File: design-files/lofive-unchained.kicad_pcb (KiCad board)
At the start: 4 copper layers, 35.6 x 17.8 mm, 39 parts, among them J1 Conn_01x09, J2 Conn_01x09, J3 USB_C_Receptacle_USB2.0, SW1 SW_Push, SW2 SW_Push, U1 ESP32-C3, U2 W25Q32JVZP, U3 TLV62569DRL, Y1 40Mhz

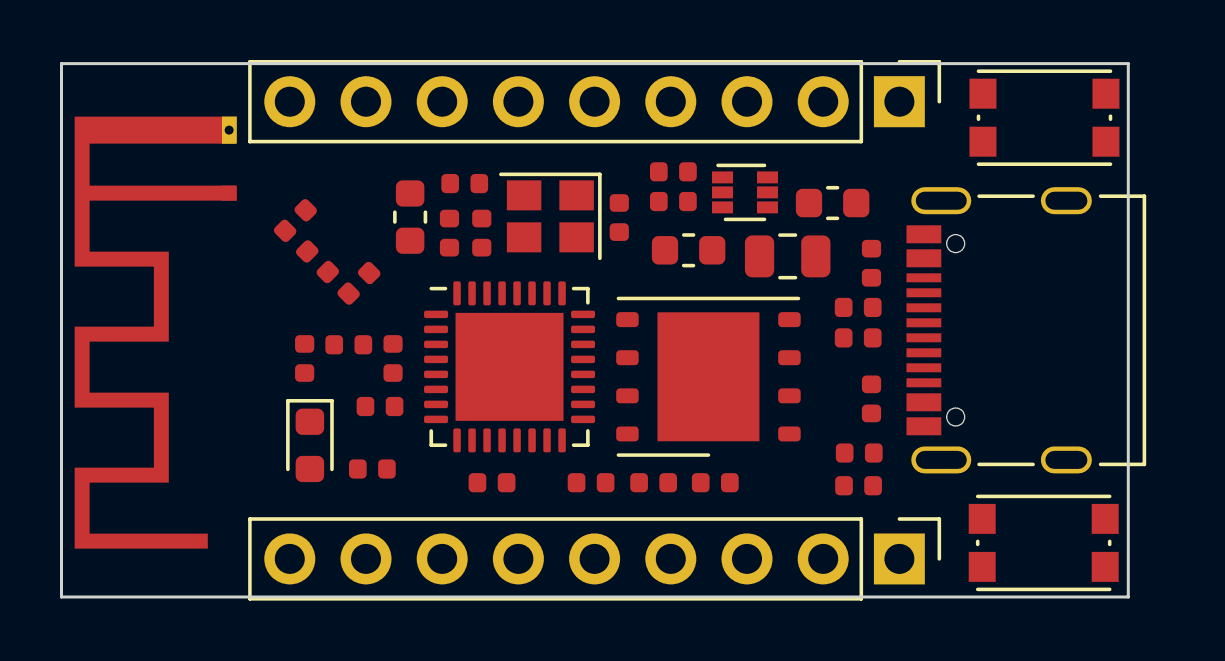
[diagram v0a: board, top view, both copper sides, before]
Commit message: Preliminary routing complete
Need to check the RF trace and USB routing.
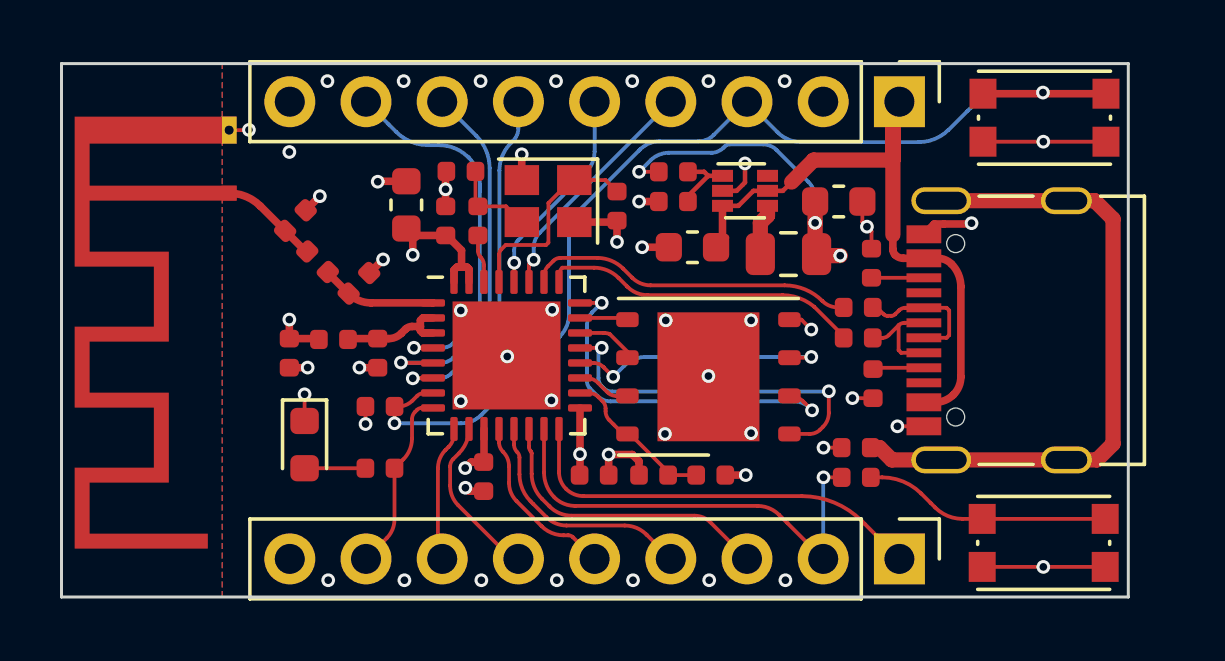
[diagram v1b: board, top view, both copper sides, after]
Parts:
- moved C6 0.54 mm to (122.3, 75.7)
- moved L1 0.54 mm to (120.8, 75.2)
- moved C3 0.54 mm to (119.4, 75.7)
- moved Y1 0.51 mm to (128.0, 70.6)
- moved R12 0.51 mm to (138.8, 76.7)
- moved C8 0.43 mm to (125.1, 69.6)
- moved R2 0.43 mm to (125.6, 71.3)
- moved C4 0.43 mm to (123.3, 70.8)
- moved C7 0.43 mm to (124.6, 71.3)
- moved U1 0.39 mm to (126.6, 75.8)
- moved C1 0.39 mm to (130.3, 70.8)
- moved C2 0.35 mm to (125.8, 79.8), turned to -90 degrees
- moved C10 0.30 mm to (133.4, 79.8)
- moved R8 0.29 mm to (138.3, 79.8)
- moved C5 0.27 mm to (129.5, 79.8)
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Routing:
- net /EN: track 0.00 -> 35.1 mm, vias 0 -> 2
- net GND: track 0.00 -> 30.6 mm, vias 0 -> 49
- net +3V3: track 0.00 -> 22.4 mm, vias 0 -> 8
- net VBUS: track 0.00 -> 22.2 mm
- net Net-(J3-PadS1): track 0.00 -> 21.9 mm
- net /GPIO9: track 0.00 -> 15.4 mm, vias 0 -> 1
- net /GPIO10: track 0.00 -> 14.0 mm
- net /GPIO0: track 0.00 -> 12.9 mm, vias 0 -> 1
- net /GPIO1: track 0.00 -> 12.4 mm, vias 0 -> 1
- net Net-(U1-Pad24): track 0.00 -> 12.3 mm, vias 0 -> 2
- net Net-(U1-Pad21): track 0.00 -> 12.1 mm, vias 0 -> 2
- net /GPIO2: track 0.00 -> 11.9 mm, vias 0 -> 1
- net Net-(R4-Pad1): track 0.00 -> 11.0 mm
- net Net-(R3-Pad1): track 0.00 -> 10.7 mm
- net /GPIO8: track 0.00 -> 10.0 mm
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- added copper zone on B.Cu, net GND
- added copper zone on F.Cu, net GND

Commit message: Switch to HRO USB connector
Available at LCSC.
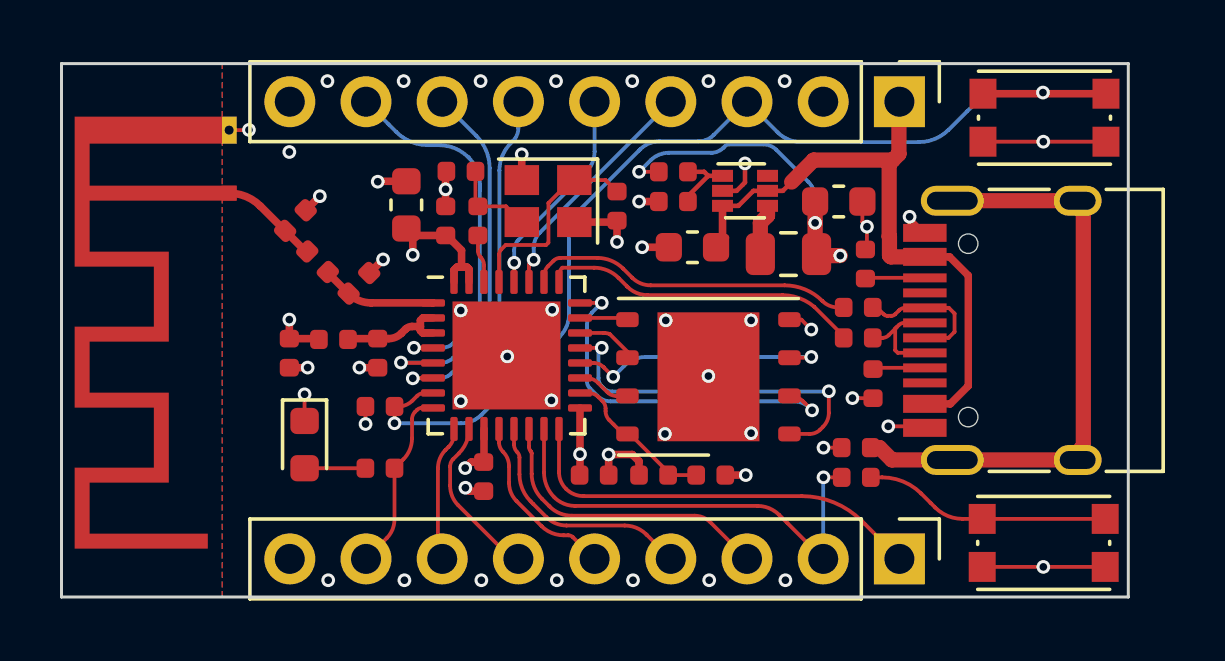
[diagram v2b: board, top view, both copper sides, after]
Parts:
- J3: footprint Connector_USB:USB_C_Receptacle_Palconn_UTC16-G -> Connector_USB:USB_C_Receptacle_HRO_TYPE-C-31-M-12
- moved J3 1.57 mm to (144.6, 74.9)
- moved R13 0.20 mm to (138.6, 72.7)
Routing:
- net Net-(J3-PadS1): track 21.9 -> 20.1 mm
- net VBUS: track 22.2 -> 21.3 mm
- net GND: track 30.6 -> 29.9 mm

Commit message: Add consummate vias and plot
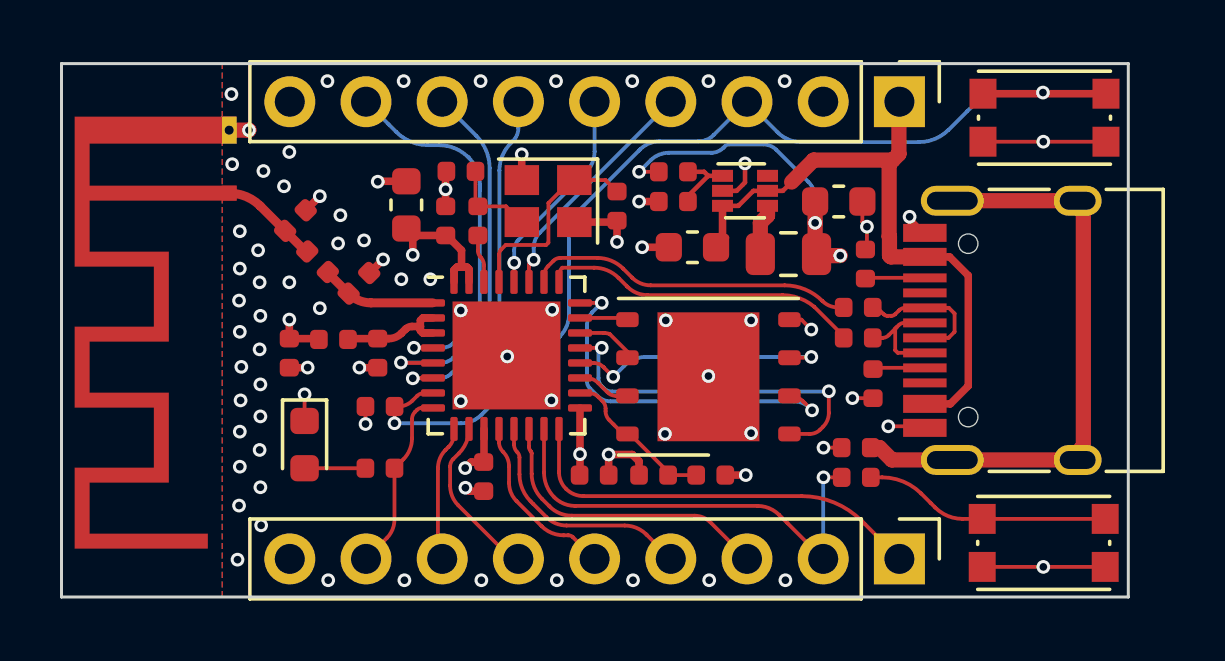
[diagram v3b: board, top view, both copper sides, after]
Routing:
- net GND: vias 49 -> 79

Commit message: Switch to 3.3V LDO instead of switcher
Signed-off-by: Michael Welling <mwelling79@gmail.com>
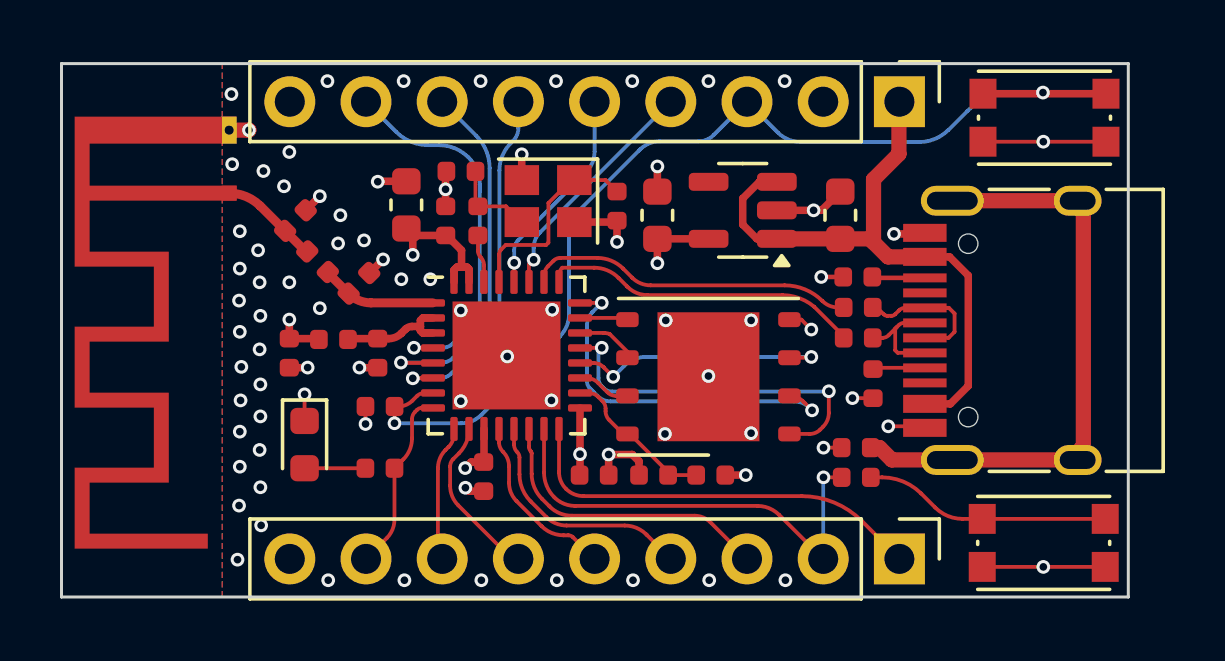
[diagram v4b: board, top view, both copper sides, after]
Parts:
- removed L3: 1.0uH, Inductor_SMD:L_0805_2012Metric
- removed R5: 210K, Resistor_SMD:R_0402_1005Metric
- removed R6: 47K, Resistor_SMD:R_0402_1005Metric
- C13: value 4.7uF -> 10uF
- C14: value 22uF -> 10uF
- U3: value TLV62569DRL -> XC6220B331MR; footprint Package_TO_SOT_SMD:SOT-563 -> Package_TO_SOT_SMD:SOT-23-5
- moved C14 6.06 mm to (131.6, 71.1), turned to 90 degrees
- moved C13 5.04 mm to (137.7, 71.1), turned to 90 degrees
- moved U3 0.65 mm to (134.5, 70.9), turned to 180 degrees
- moved R13 0.50 mm to (138.3, 73.2), turned to 0 degrees
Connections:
- U3 pad 1: Net-(R5-Pad1) -> VBUS
- U3 pad 4: Net-(L3-Pad1) -> unconnected-(U3-NC-Pad4)
- U3 pad 5: VBUS -> +3V3
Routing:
- net +3V3: track 22.4 -> 13.8 mm, vias 8 -> 6
- net Net-(R5-Pad1): track 2.34 -> 0.00 mm
- net Net-(L3-Pad1): track 1.55 -> 0.00 mm
- net GND: track 29.9 -> 29.4 mm, vias 79 -> 78
